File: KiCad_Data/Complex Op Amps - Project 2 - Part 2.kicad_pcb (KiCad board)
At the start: 2 copper layers, 184.2 x 82.1 mm, 121 parts, among them P1 Potentiometer P/N: 3590P-2-**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, P2 Potentiometer P/N: 3590P-2-**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, SW1 SPST Switch, P/N: GT12MABE, SW2 SPST Switch, P/N: GT12MABE, SW3 SPST Switch, P/N: GT12MABE, SW4 SPST Switch, P/N: GT12MABE, SW5 SPST Switch, P/N: GT12MABE, T1 Transistor P/N: 2N3906, T2 Transistor P/N: 2N3906, T3 Transistor P/N: 2N3906, T4 Transistor P/N: 2N3906

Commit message: Updated PCB and Schematic
The PCB has the same changes as the schematic, the schematic had the DPDT switch made into 2 separate switches and capacitors were added onto the DG201 switch's
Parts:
- removed D_SW1: P/N: 7101SD9AV2BE, Complex_Op_Amps_Footprints:DPDT Switch
- added NC25: Normal_Capacitor, P/N: 399-4209-ND, Complex_Op_Amps_Footprints:CAPACITOR - 399-4209-ND, F.Cu at (80.4, 96.0)
- added NC26: Normal_Capacitor, P/N: 399-4209-ND, Complex_Op_Amps_Footprints:CAPACITOR - 399-4209-ND, F.Cu at (101.1, 114.4)
- added SW6: SPDT Switch, P/N: 7101SD9AV2BE, Complex_Op_Amps_Footprints:AV2_Switch, F.Cu at (52.4, 154.3)
- added SW7: SPDT Switch, P/N: 7101SD9AV2BE, Complex_Op_Amps_Footprints:AV2_Switch, F.Cu at (61.5, 154.3)
- SW1, SW2, SW3, SW4, SW5: value SPST Switch, P/N: GT12MABE -> SPDT Switch, P/N: 7101SD9AV2BE
- moved R29 12.7 mm to (137.2, 118.3)
- moved NC21 11.6 mm to (130.3, 117.1)
- moved NC5 8.76 mm to (84.5, 89.8)
- moved R7 7.38 mm to (87.2, 101.2)
- moved TP5 7.38 mm to (87.2, 98.6)
- moved R27 5.49 mm to (123.7, 120.9)
- moved SW1 2.56 mm to (70.6, 154.3)
- moved SW3 2.56 mm to (117.1, 154.3)
- moved P1 2.56 mm to (78.8, 135.3)
- moved TrimP1 2.56 mm to (129.2, 147.0)
- moved TrimP2 2.56 mm to (105.0, 147.0)
- moved TrimP3 2.56 mm to (112.2, 147.0)
- moved NC16 2.04 mm to (53.2, 112.6)
- moved NC13 1.80 mm to (189.6, 97.6)
- moved TP8 1.70 mm to (142.4, 111.7)
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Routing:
- net -15V: track 827.4 -> 931.9 mm, vias 0 -> 3
- net Net-(SW1-C): track 296.5 -> 322.6 mm, vias 3 -> 4
- net Net-(SW6-A): track 170.1 -> 153.7 mm, vias 1 -> 0
- net Net-(TR2-B): track 196.5 -> 180.7 mm
- net Net-(OPAMP10-Pad6): track 13.4 -> 28.4 mm
- net +15V: track 756.9 -> 771.3 mm, vias 0 -> 1
- net Net-(IDC1-C-Pad7): track 91.3 -> 78.9 mm, vias 0 -> 2
- net Net-(T1-B): track 187.4 -> 199.8 mm
- net Net-(DG1A-S1): track 220.0 -> 230.7 mm
- net Net-(OPAMP10--): track 33.1 -> 42.8 mm
- net Net-(OPAMP9-+): track 110.6 -> 119.4 mm
- net Net-(DG1B-S2): track 249.5 -> 241.6 mm
- net Net-(SW1-B): track 70.1 -> 76.1 mm
- net -5V: track 221.3 -> 215.4 mm
- net Net-(DG1A-D1): track 148.1 -> 154.0 mm, vias 0 -> 1
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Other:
- board text added: "Current Out"
- board text added: "Error Signal"
- board text added: "Piezo Out"
- board text added: "Piezo Ramp"

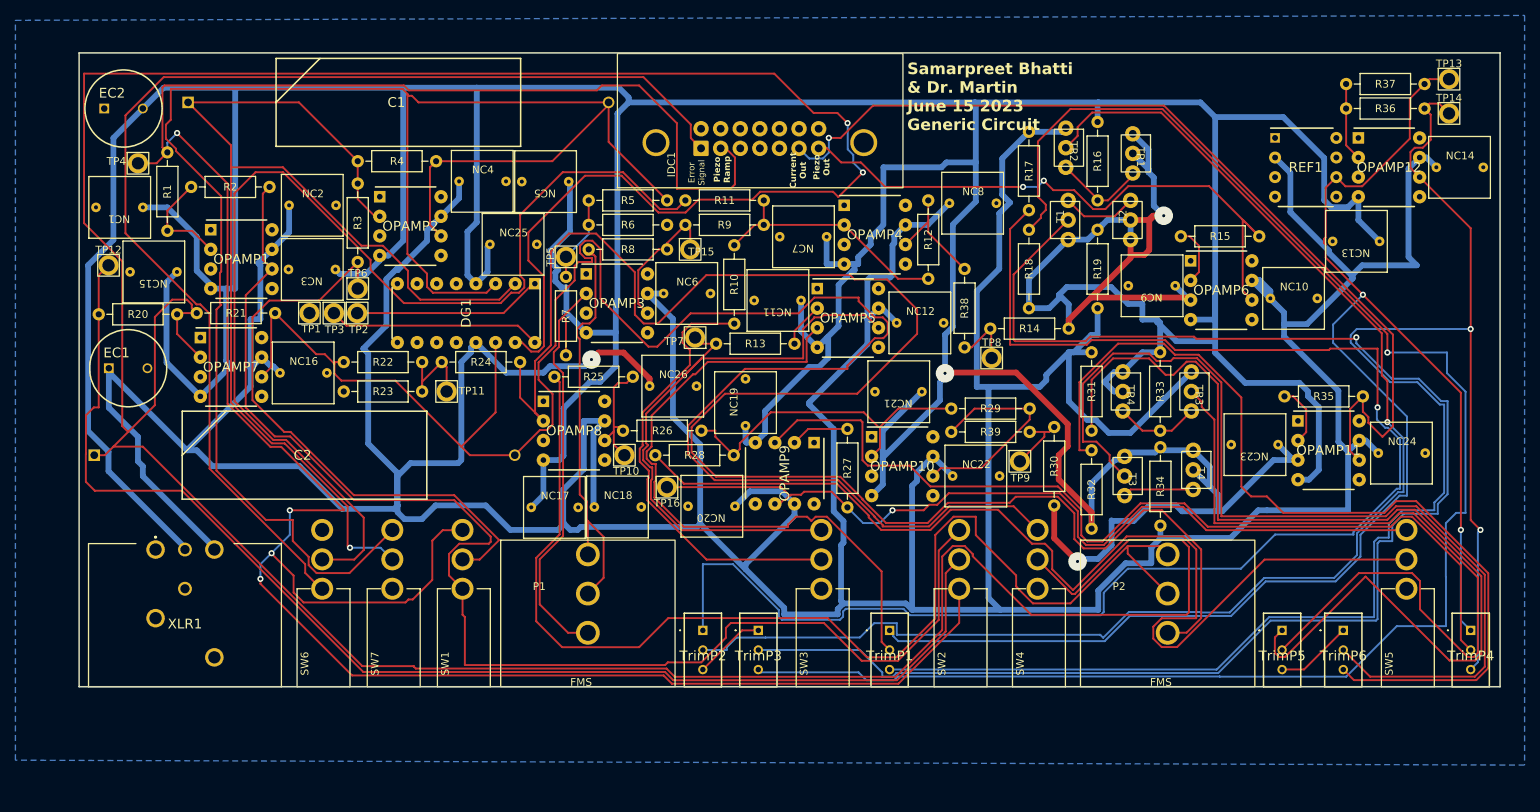
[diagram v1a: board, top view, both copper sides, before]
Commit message: Fixed minor DRC issue with clearance
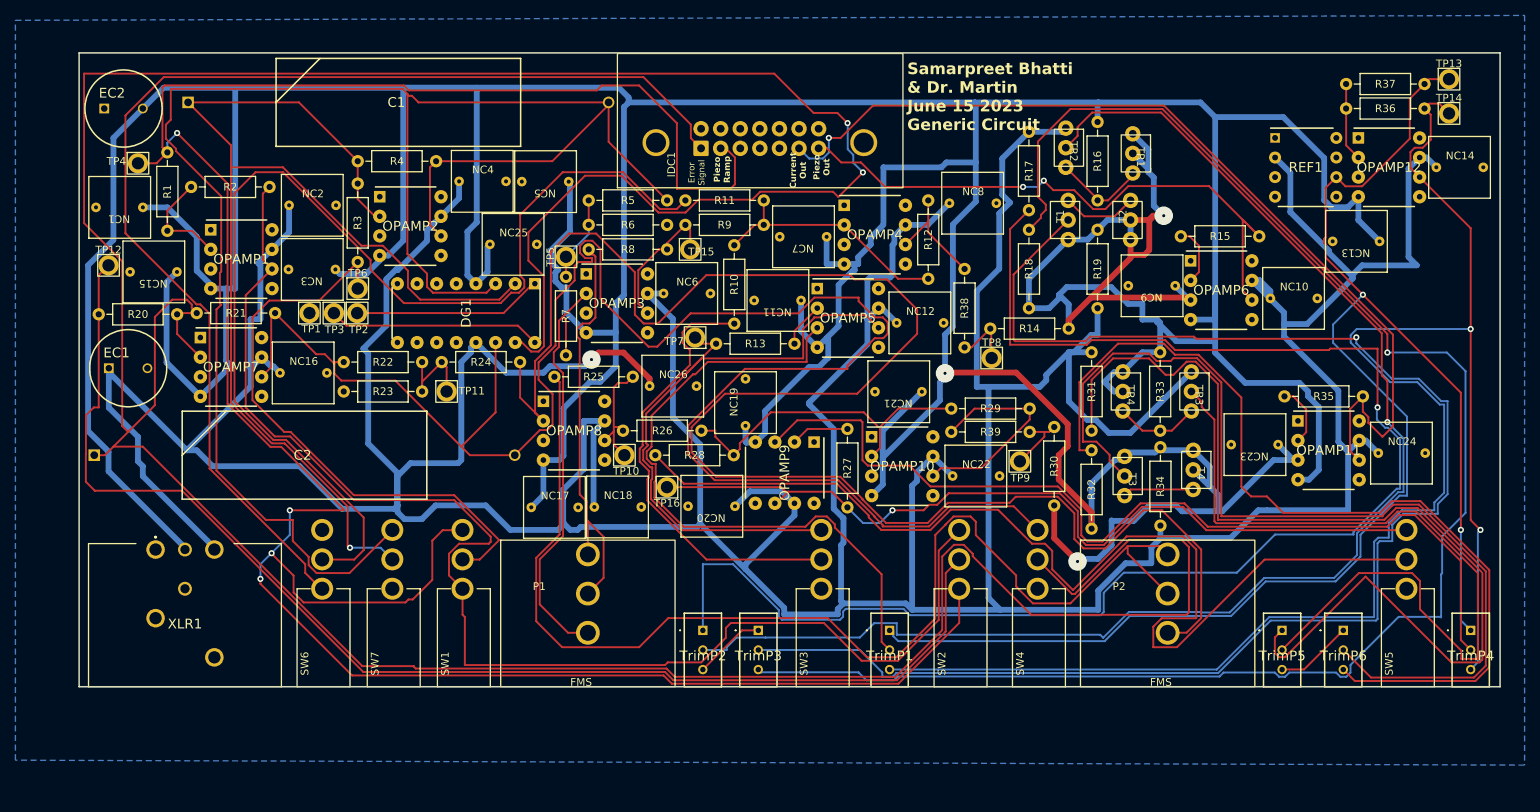
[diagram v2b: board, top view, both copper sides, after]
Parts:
- moved OPAMP9 0.08 mm to (115.6, 126.6)
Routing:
- net Net-(TR3-B): track 102.6 -> 104.3 mm
- net Net-(R31-Pad2): track 132.3 -> 133.5 mm
- net Net-(T3-B): track 124.6 -> 125.4 mm
- net Net-(SW5-B): track 139.1 -> 139.7 mm
- net Net-(OPAMP5-+): track 85.4 -> 84.9 mm
- net Net-(R32-Pad1): track 118.1 -> 118.7 mm
